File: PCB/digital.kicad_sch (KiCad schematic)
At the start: 18 parts, among them J3 JTAG, J4 ICSP, U2 PIC32MK0256MCJ048-I/Y8X, Y1 ECS-3225SMV-080-GP-TR, Y2 ECS-3225SMV-080-GP-TR

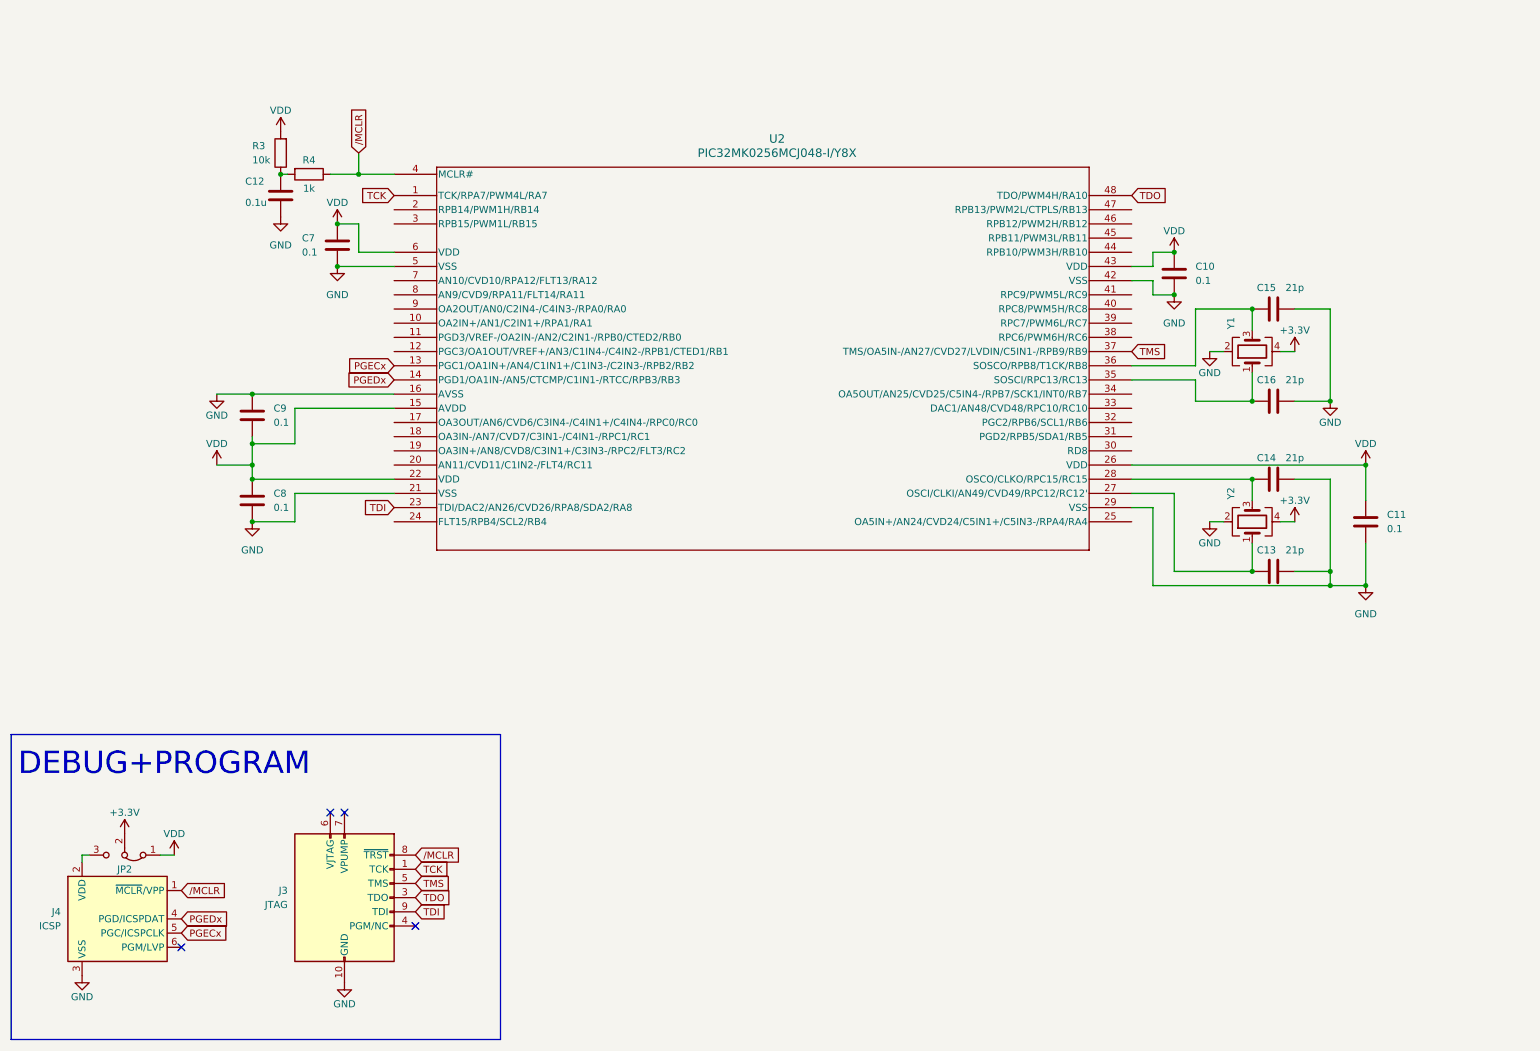
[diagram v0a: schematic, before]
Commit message: falta RFID i final de carrera
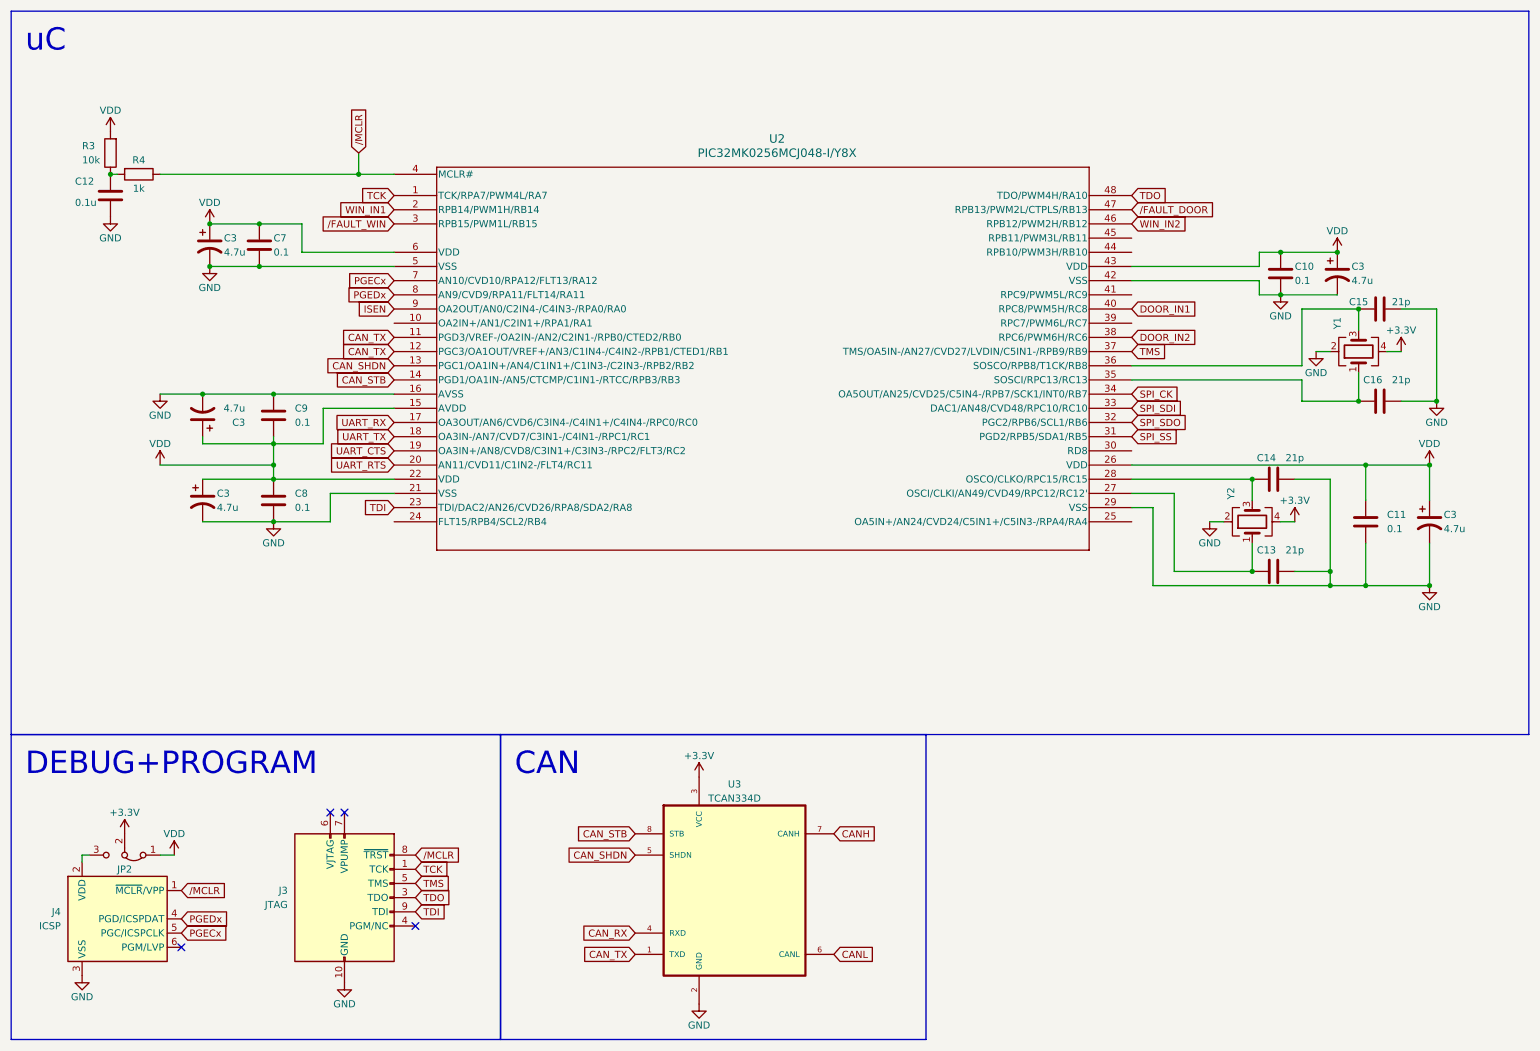
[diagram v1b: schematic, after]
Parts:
- added C3 (x5): 4.7u, symbol Device:C_Polarized_US
- added U3: TCAN334D, symbol TCAN3413DR:TCAN334D
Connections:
- net +3.3V: now also U3.3 (VCC)
- net GND: now also C3.2, C3.2, C3.2, C3.2, C3.2, U3.2 (GND)
- net PGECx: now also U2.7 (AN10/CVD10/RPA12/FLT13/RA12); no longer U2.13 (PGC1/OA1IN+/AN4/C1IN1+/C1IN3-/C2IN3-/RPB2/RB2)
- net PGEDx: now also U2.8 (AN9/CVD9/RPA11/FLT14/RA11); no longer U2.14 (PGD1/OA1IN-/AN5/CTCMP/C1IN1-/RTCC/RPB3/RB3)
- net VDD: now also C3.1, C3.1, C3.1, C3.1, C3.1
- net CAN_TX: now reaches U2.11 (PGD3/VREF-/OA2IN-/AN2/C2IN1-/RPB0/CTED2/RB0)
- net CAN_TX: now also U2.12 (PGC3/OA1OUT/VREF+/AN3/C1IN4-/C4IN2-/RPB1/CTED1/RB1), U3.1 (TXD)
- net UART_RX: now reaches U2.17 (OA3OUT/AN6/CVD6/C3IN4-/C4IN1+/C4IN4-/RPC0/RC0)
- net UART_TX: now reaches U2.18 (OA3IN-/AN7/CVD7/C3IN1-/C4IN1-/RPC1/RC1)
- net UART_CTS: now reaches U2.19 (OA3IN+/AN8/CVD8/C3IN1+/C3IN3-/RPC2/FLT3/RC2)
- net WIN_IN1: now reaches U2.2 (RPB14/PWM1H/RB14)
- net UART_RTS: now reaches U2.20 (AN11/CVD11/C1IN2-/FLT4/RC11)
- net /FAULT_WIN: now reaches U2.3 (RPB15/PWM1L/RB15)
- net SPI_SS: now reaches U2.31 (PGD2/RPB5/SDA1/RB5)
- net SPI_SDO: now reaches U2.32 (PGC2/RPB6/SCL1/RB6)
- net SPI_SDI: now reaches U2.33 (DAC1/AN48/CVD48/RPC10/RC10)
- net SPI_CK: now reaches U2.34 (OA5OUT/AN25/CVD25/C5IN4-/RPB7/SCK1/INT0/RB7)
- net DOOR_IN2: now reaches U2.38 (RPC6/PWM6H/RC6)
- net DOOR_IN1: now reaches U2.40 (RPC8/PWM5H/RC8)
- net WIN_IN2: now reaches U2.46 (RPB12/PWM2H/RB12)
- net /FAULT_DOOR: now reaches U2.47 (RPB13/PWM2L/CTPLS/RB13)
- net ISEN: now reaches U2.9 (OA2OUT/AN0/C2IN4-/C4IN3-/RPA0/RA0)
- new net CANH: U3.7 (CANH)
- new net CANL: U3.6 (CANL)
- new net CAN_RX: U3.4 (RXD)
- new net CAN_SHDN: U2.13 (PGC1/OA1IN+/AN4/C1IN1+/C1IN3-/C2IN3-/RPB2/RB2), U3.5 (SHDN)
- new net CAN_STB: U2.14 (PGD1/OA1IN-/AN5/CTCMP/C1IN1-/RTCC/RPB3/RB3), U3.8 (STB)
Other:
- note added: "CAN"
- note added: "uC"
- moved on the sheet: C10, C12, C15, C16, C7, C8, C9, R3, R4, Y1

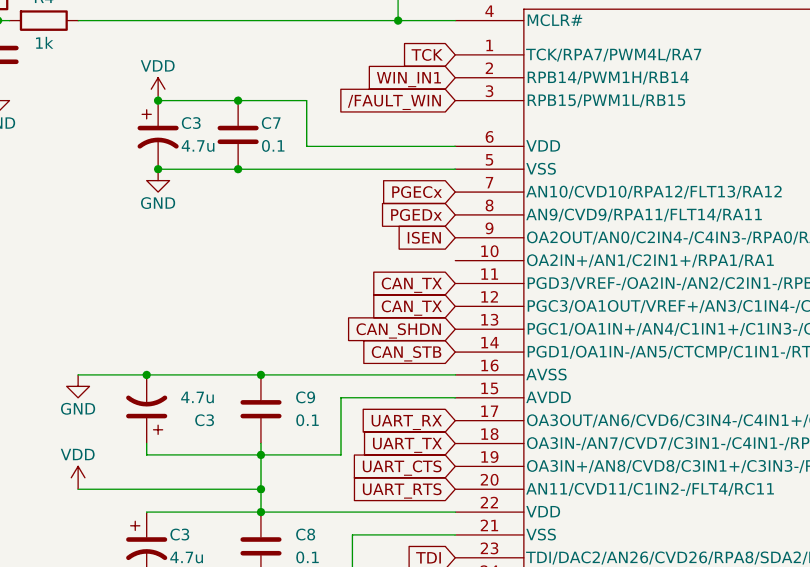
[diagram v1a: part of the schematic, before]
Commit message: change RX to TX error
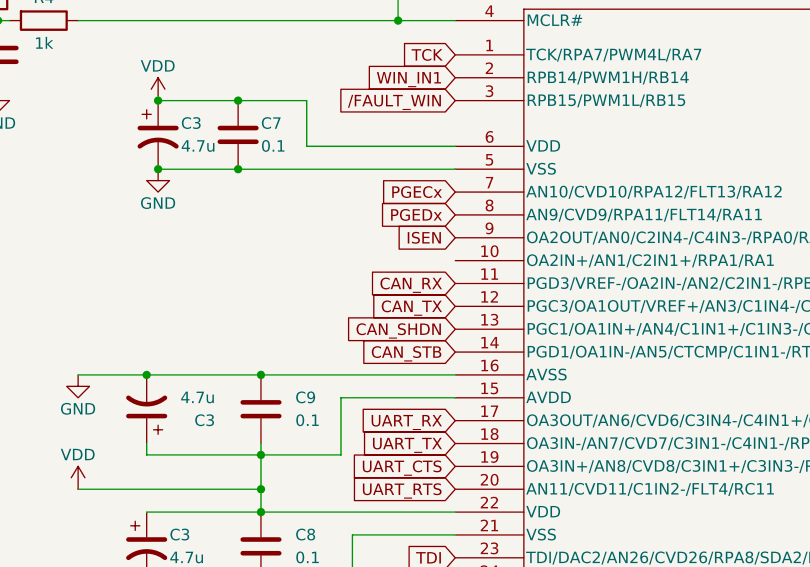
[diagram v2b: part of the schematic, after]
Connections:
- net CAN_RX: now also U2.11 (PGD3/VREF-/OA2IN-/AN2/C2IN1-/RPB0/CTED2/RB0)
- net CAN_TX: no longer U2.11 (PGD3/VREF-/OA2IN-/AN2/C2IN1-/RPB0/CTED2/RB0)
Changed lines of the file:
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@@
     )
   )
-  (global_label "CAN_TX" (shape input) (at 81.28 71.12 180) (fields_autoplaced)
+  (global_label "CAN_RX" (shape input) (at 81.28 71.12 180) (fields_autoplaced)
     (effects (font (size 1.27 1.27)) (justify right))
-    (property "Intersheetrefs" "${INTERSHEET_REFS}" (at 71.5404 71.12 0)
+    (property "Intersheetrefs" "${INTERSHEET_REFS}" (at 71.238 71.12 0)
       (effects (font (size 1.27 1.27)) (justify right) hide)
     )

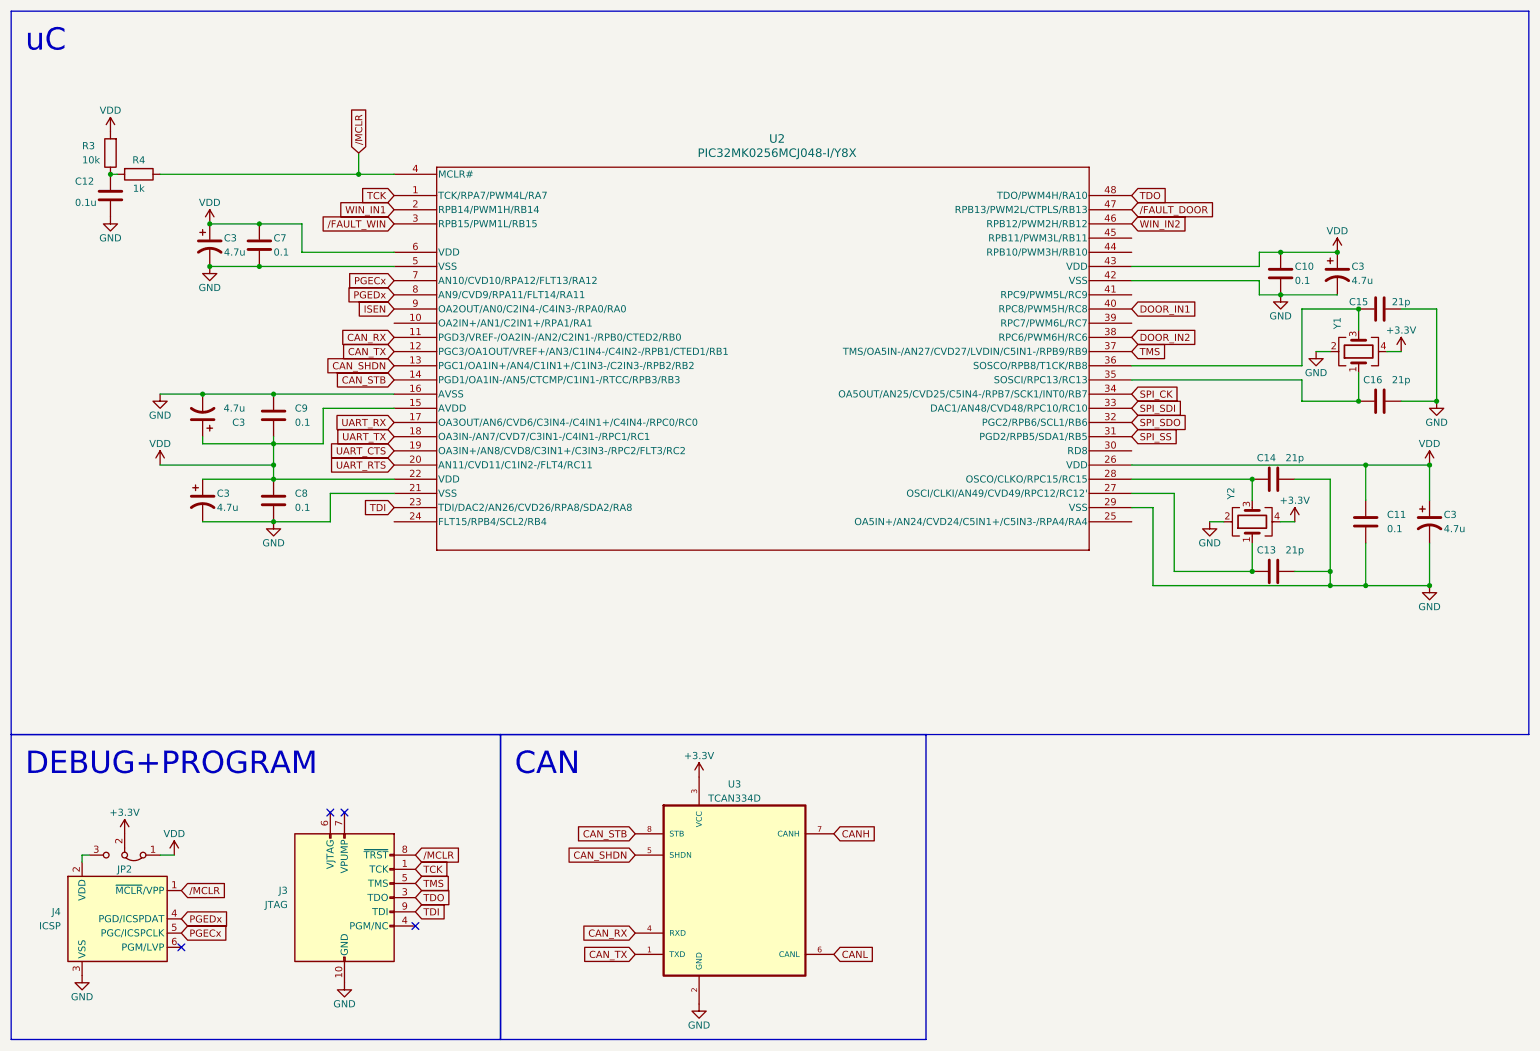
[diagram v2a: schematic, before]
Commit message: correct schematic + README
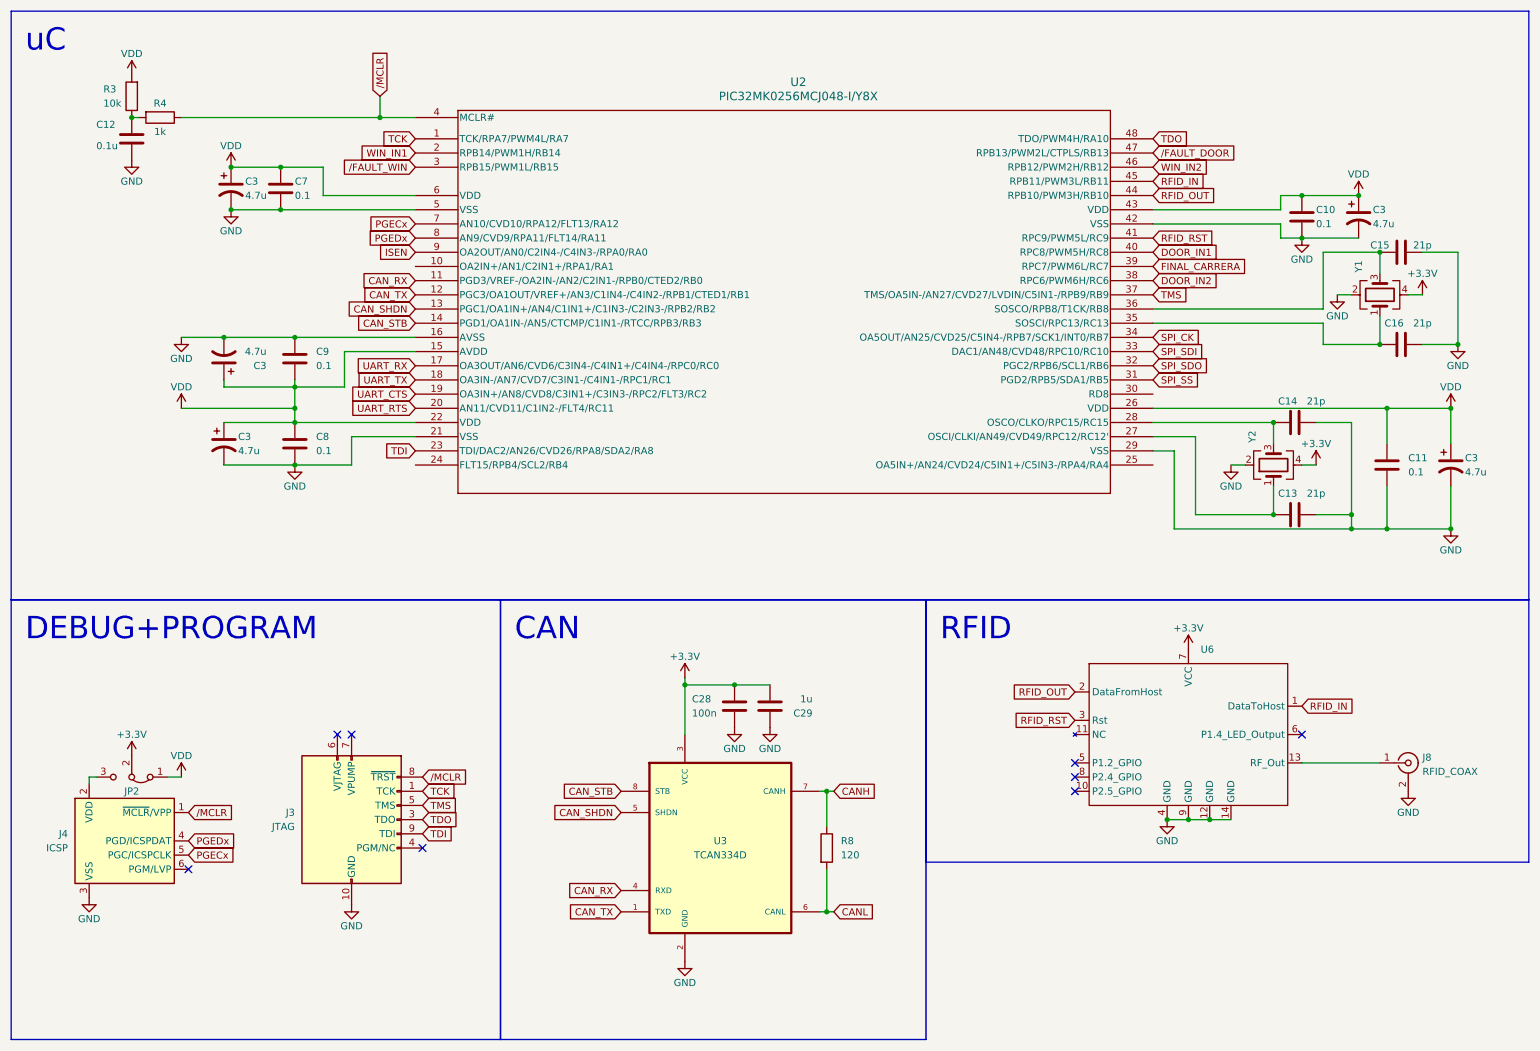
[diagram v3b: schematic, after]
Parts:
- added C28: 100n, symbol Device:C
- added C29: 1u, symbol Device:C
- added J8: RFID_COAX, symbol Connector:Conn_Coaxial
- added R8: 120, symbol Device:R
- added U6: ~, symbol DLP-RFID2:DLP-RFID2
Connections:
- net +3.3V: now also C28.2, C29.1, U6.7 (VCC)
- net CANH: now also R8.1
- net CANL: now also R8.2
- net GND: now also C28.1, C29.2, J8.2 (Ext), U6.12 (GND), U6.14 (GND), U6.4 (GND), U6.9 (GND)
- net FINAL_CARRERA: now reaches U2.39 (RPC7/PWM6L/RC7)
- net RFID_RST: now reaches U2.41 (RPC9/PWM5L/RC9)
- net RFID_RST: now also U6.3 (Rst)
- net RFID_OUT: now reaches U2.44 (RPB10/PWM3H/RB10)
- net RFID_OUT: now also U6.2 (DataFromHost)
- net RFID_IN: now reaches U2.45 (RPB11/PWM3L/RB11)
- net RFID_IN: now also U6.1 (DataToHost)
- new net: J8.1 (In), U6.13 (RF_Out)
- no-connect marks 4 -> 8
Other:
- note added: "RFID"
- moved on the sheet: C10, C11, C12, C13, C14, C15, C16, C3, C7, C8, C9, J3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

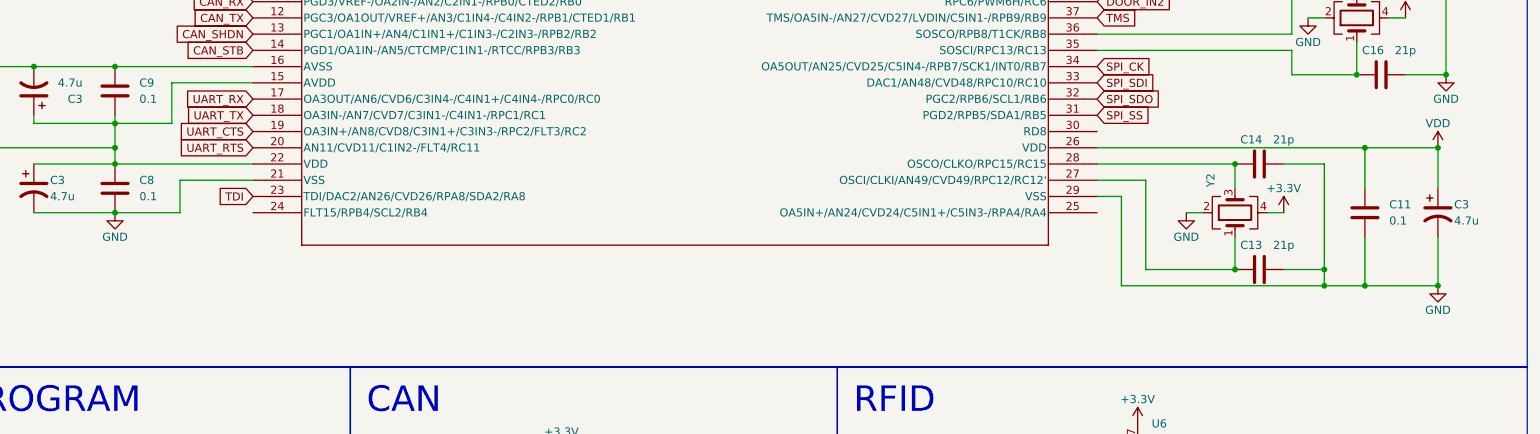
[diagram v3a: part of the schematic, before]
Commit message: add button controls
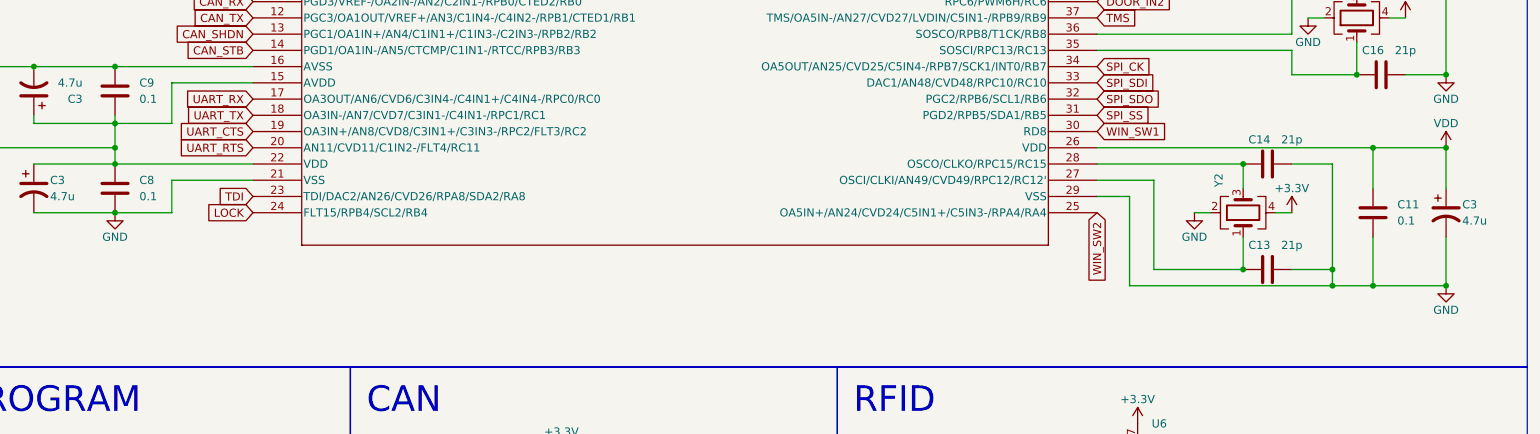
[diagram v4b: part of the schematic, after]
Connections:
- net LOCK: now reaches U2.24 (FLT15/RPB4/SCL2/RB4)
- net WIN_SW2: now reaches U2.25 (OA5IN+/AN24/CVD24/C5IN1+/C5IN3-/RPA4/RA4)
- net WIN_SW1: now reaches U2.30 (RD8)
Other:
- moved on the sheet: C11, C13, C14, C3, Y2
